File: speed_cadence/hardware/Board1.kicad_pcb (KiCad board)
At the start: 2 copper layers, 29.9 x 37.4 mm, 11 parts, among them IC1 AH1912-W-7, J1 DX07S016JA3R1500, J2 Conn_01x04_Pin, SW1 SW_Push, U1 STM32F042G6U6TR, U2 TS2940CW33_RPG

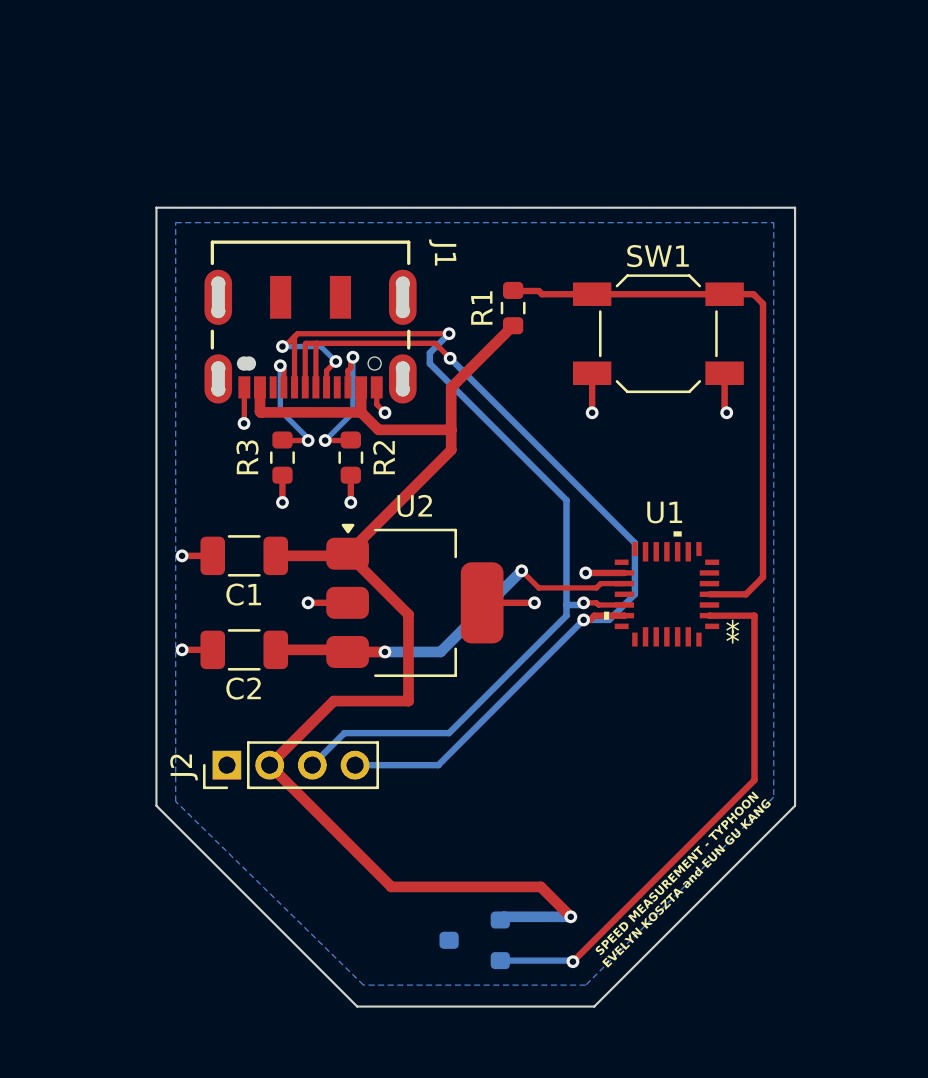
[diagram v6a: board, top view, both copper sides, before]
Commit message: Added mounting holes
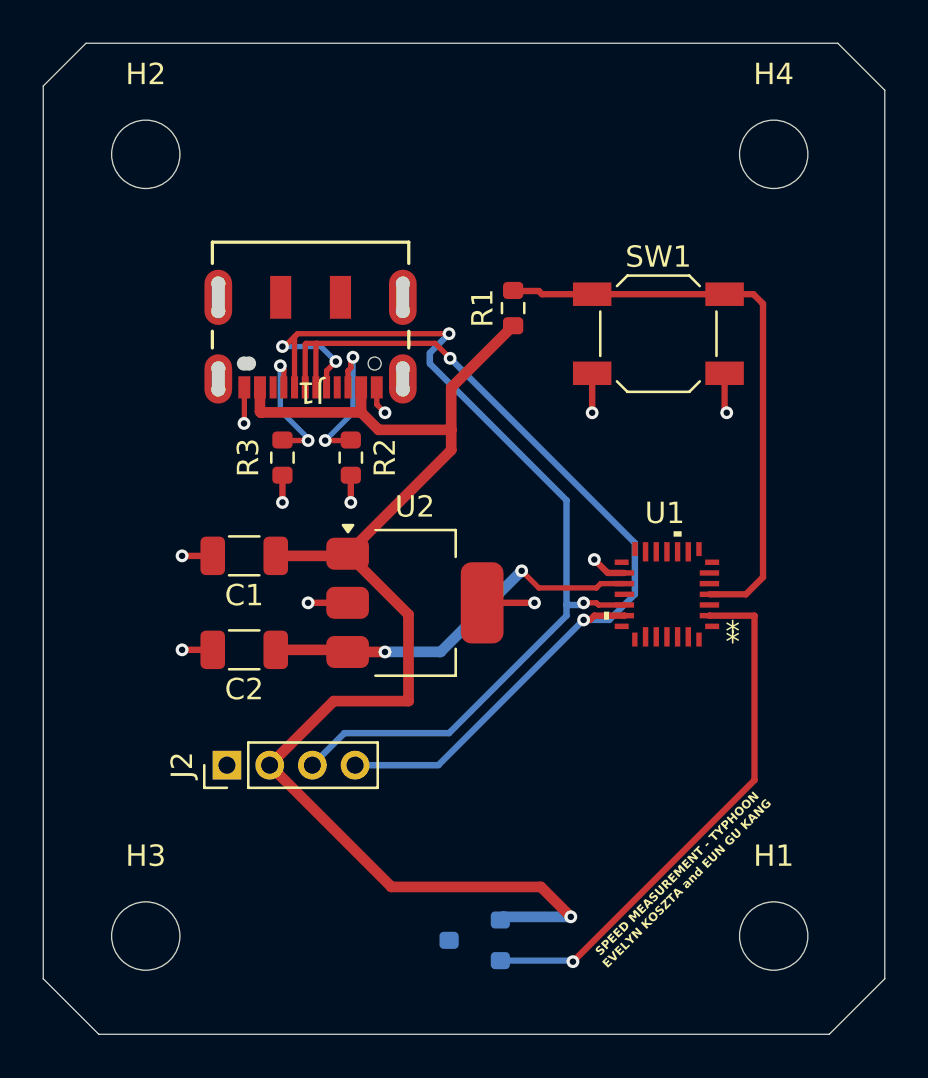
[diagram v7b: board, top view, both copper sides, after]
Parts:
- added H1: MountingHole, MountingHole:MountingHole_3.2mm_M3_ISO14580, F.Cu at (103.0, 93.4)
- added H2: MountingHole, MountingHole:MountingHole_3.2mm_M3_ISO14580, F.Cu at (73.6, 56.8)
- added H3: MountingHole, MountingHole:MountingHole_3.2mm_M3_ISO14580, F.Cu at (73.6, 93.4)
- added H4: MountingHole, MountingHole:MountingHole_3.2mm_M3_ISO14580, F.Cu at (103.0, 56.8)
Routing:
- removed copper zone on B.Cu, net GND
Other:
- board size 29.9 x 37.4 mm -> 39.4 x 46.4 mm

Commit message: Re-added the GND fill
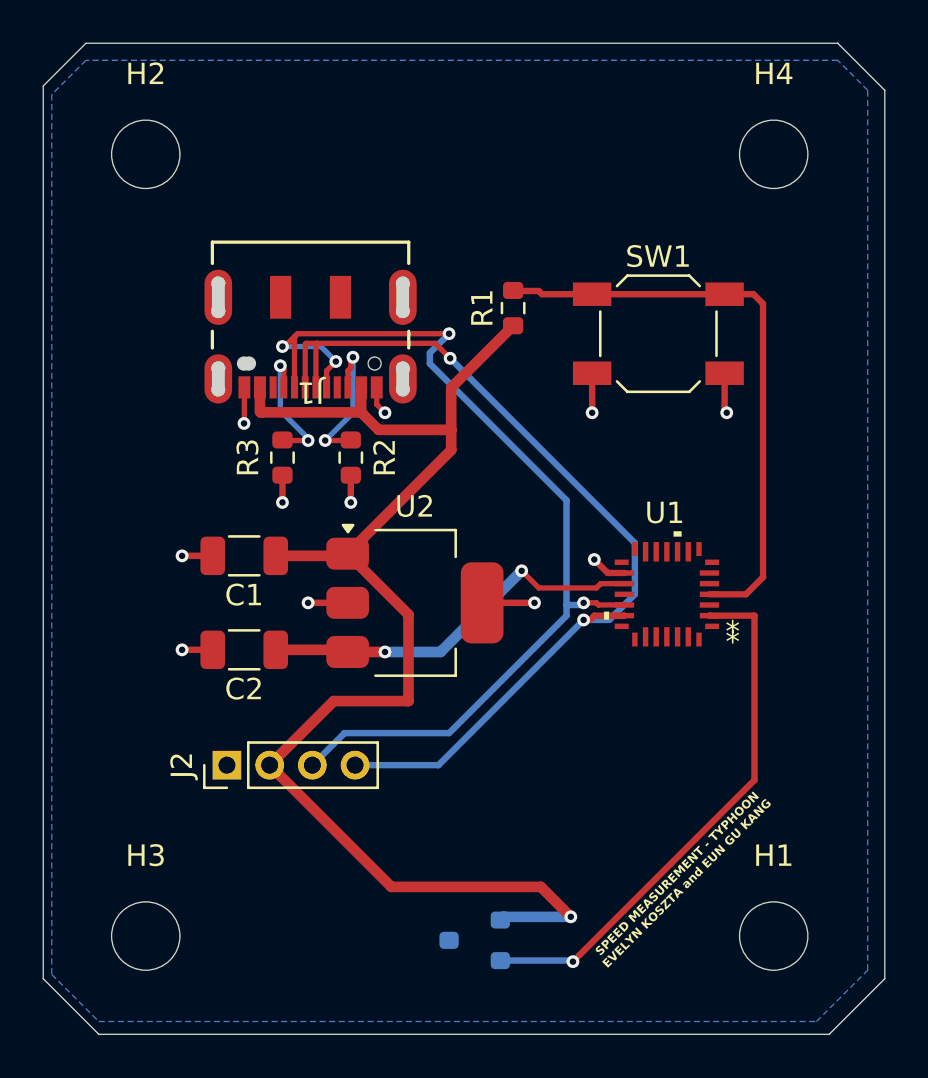
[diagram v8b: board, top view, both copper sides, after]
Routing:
- added copper zone on B.Cu, net GND
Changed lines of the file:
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@@
 			)
 		)
-		(property "Footprint" "CONN12_DX07S_JAE"
+		(property "Footprint" "DX07S016JA3R1500_USBC:CONN12_DX07S_JAE"
 			(at 0 0 180)
 			(unlocked yes)
@@
 		(net 33)
 	)
+	(zone
+		(net 2)
+		(net_name "GND")
+		(layer "B.Cu")
+		(hatch edge 0.5)
+		(connect_pads
+			(clearance 0.5)
+		)
+		(min_thickness 0.25)
+		(filled_areas_thickness no)
+		(fill yes
+			(thermal_gap 0.5)
+			(thermal_bridge_width 0.5)
+		)
+		(polygon
+			(pts
+				(xy 106 52.4) (xy 70.8 52.4) (xy 69.2 54) (xy 69.2 95.2) (xy 71.4 97.4) (xy 105 97.4) (xy 107.4 95)
+				(xy 107.4 53.8)
+			)
+		)
+	)
 )
